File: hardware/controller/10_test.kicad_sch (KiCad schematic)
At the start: 4 parts

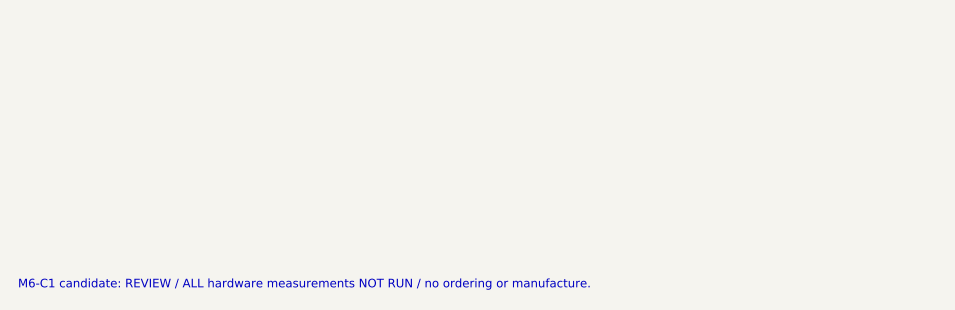
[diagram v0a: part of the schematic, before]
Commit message: M6-C1R1: protect pack identity input and review USB ESD topology
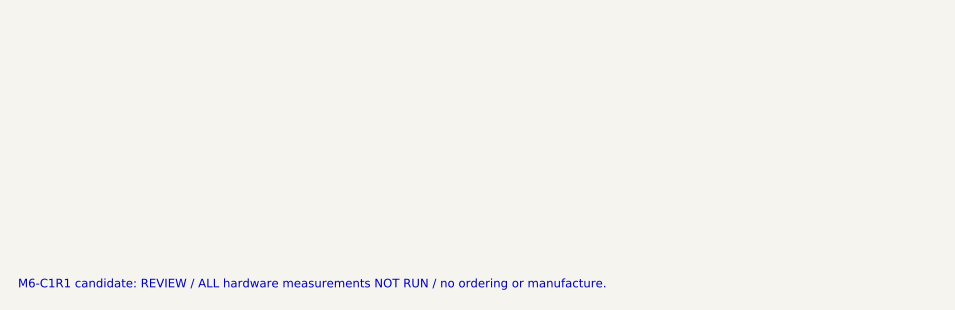
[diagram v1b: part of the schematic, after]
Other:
- note added: "M6-C1R1 candidate: REVIEW / ALL hardware measurements NOT RUN / no ordering or manufacture."
- note removed: "M6-C1 candidate: REVIEW / ALL hardware measurements NOT RUN / no ordering or manufacture."
